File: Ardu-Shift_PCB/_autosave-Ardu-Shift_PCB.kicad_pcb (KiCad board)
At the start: 2 copper layers, 101.6 x 66 mm, 18 parts, among them U1 OLED(SPI), U2 Arduino_Pro_Micro

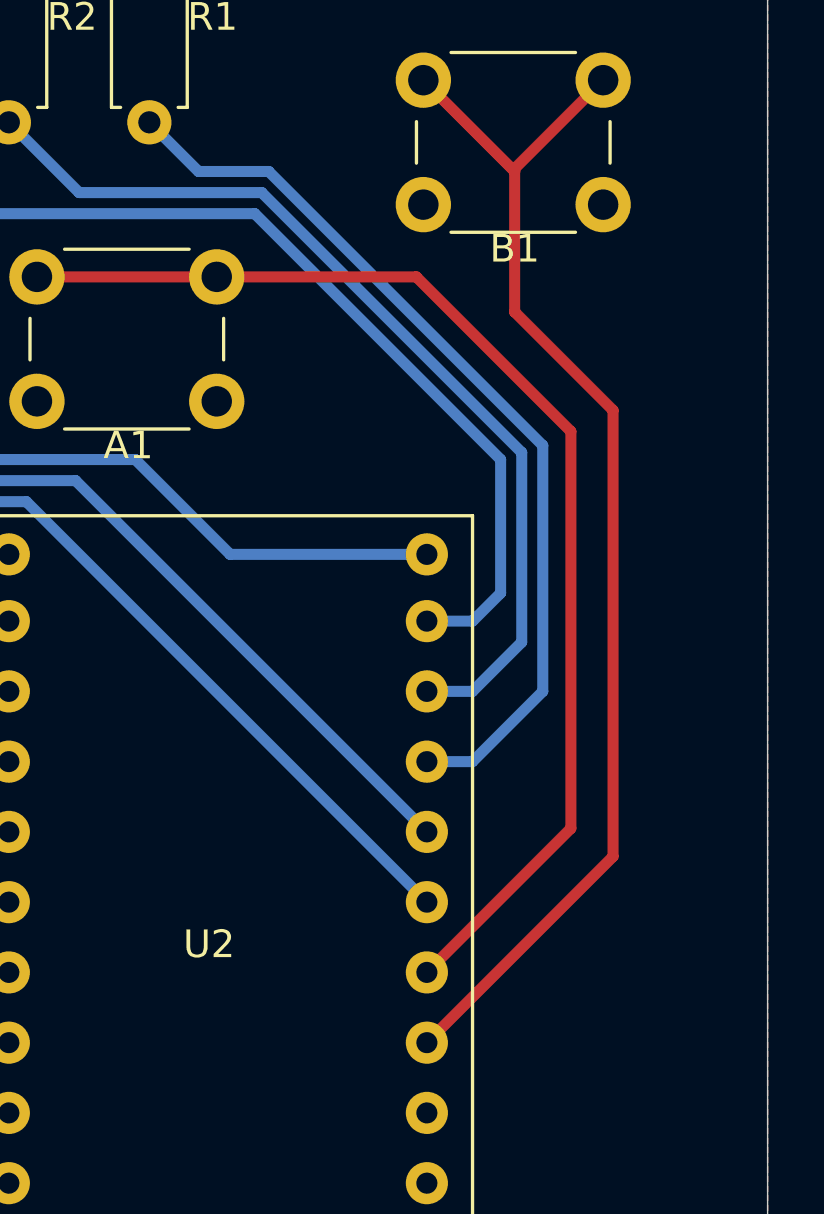
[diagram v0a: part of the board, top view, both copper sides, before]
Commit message: first version of the final assembly/routing of game-device PCB
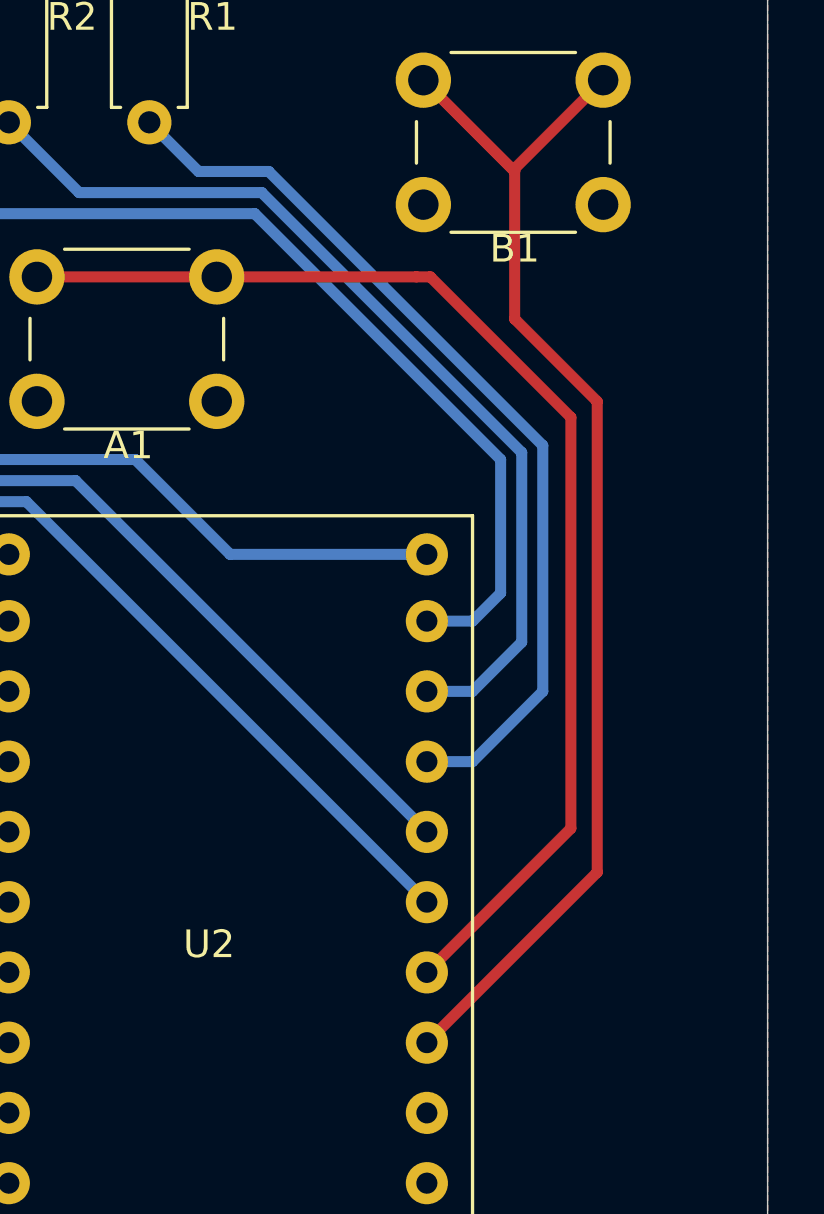
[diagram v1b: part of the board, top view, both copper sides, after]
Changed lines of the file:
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@@
     (thickness 1.6)
     (drawings 54)
-    (tracks 110)
+    (tracks 111)
     (zones 0)
     (modules 18)
@@
       (padsonsilk false)
       (subtractmaskfromsilk false)
-      (outputformat 1)
+      (outputformat 4)
       (mirror false)
-      (drillshape 1)
+      (drillshape 0)
       (scaleselection 1)
       (outputdirectory ""))
@@
   (segment (start 93.98 90.424) (end 93.98 94.996) (width 0.4) (layer F.Cu) (net 24))
   (segment (start 110.744 58.928) (end 117.244 58.928) (width 0.4) (layer F.Cu) (net 26))
-  (segment (start 117.244 58.928) (end 124.46 58.928) (width 0.4) (layer F.Cu) (net 26))
-  (segment (start 124.46 58.928) (end 130.048 64.516) (width 0.4) (layer F.Cu) (net 26))
-  (segment (start 130.048 78.867) (end 124.841 84.074) (width 0.4) (layer F.Cu) (net 26))
-  (segment (start 130.048 64.516) (end 130.048 78.867) (width 0.4) (layer F.Cu) (net 26))
-  (segment (start 124.841 86.614) (end 131.572 79.883) (width 0.4) (layer F.Cu) (net 27))
-  (segment (start 131.572 79.883) (end 131.572 63.754) (width 0.4) (layer F.Cu) (net 27))
-  (segment (start 131.572 63.754) (end 128.016 60.198) (width 0.4) (layer F.Cu) (net 27))
+  (segment (start 124.46 58.928) (end 117.244 58.928) (width 0.4) (layer F.Cu) (net 26))
+  (segment (start 124.968 58.928) (end 124.46 58.928) (width 0.4) (layer F.Cu) (net 26))
+  (segment (start 130.048 64.008) (end 124.968 58.928) (width 0.4) (layer F.Cu) (net 26))
+  (segment (start 130.048 78.867) (end 130.048 64.008) (width 0.4) (layer F.Cu) (net 26))
+  (segment (start 124.841 84.074) (end 130.048 78.867) (width 0.4) (layer F.Cu) (net 26))
   (segment (start 128.016 55.118) (end 124.714 51.816) (width 0.4) (layer F.Cu) (net 27))
-  (segment (start 128.016 60.198) (end 128.016 55.118) (width 0.4) (layer F.Cu) (net 27))
   (segment (start 128.016 55.014) (end 128.016 55.118) (width 0.4) (layer F.Cu) (net 27))
   (segment (start 131.214 51.816) (end 128.016 55.014) (width 0.4) (layer F.Cu) (net 27))
+  (segment (start 131.0005 63.4365) (end 131.0005 80.4545) (width 0.4) (layer F.Cu) (net 27))
+  (segment (start 128.016 60.452) (end 131.0005 63.4365) (width 0.4) (layer F.Cu) (net 27))
+  (segment (start 128.016 55.118) (end 128.016 60.452) (width 0.4) (layer F.Cu) (net 27))
+  (segment (start 124.841 86.614) (end 131.0005 80.4545) (width 0.4) (layer F.Cu) (net 27))
   (zone (net 10) (net_name GND) (layer B.Cu) (hatch edge 0.508)
     (connect_pads (clearance 0.508))
